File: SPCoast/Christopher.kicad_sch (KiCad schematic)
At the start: 42 parts, among them SW9813 813, SW9815 815, SW9817 817, SW9900 815A

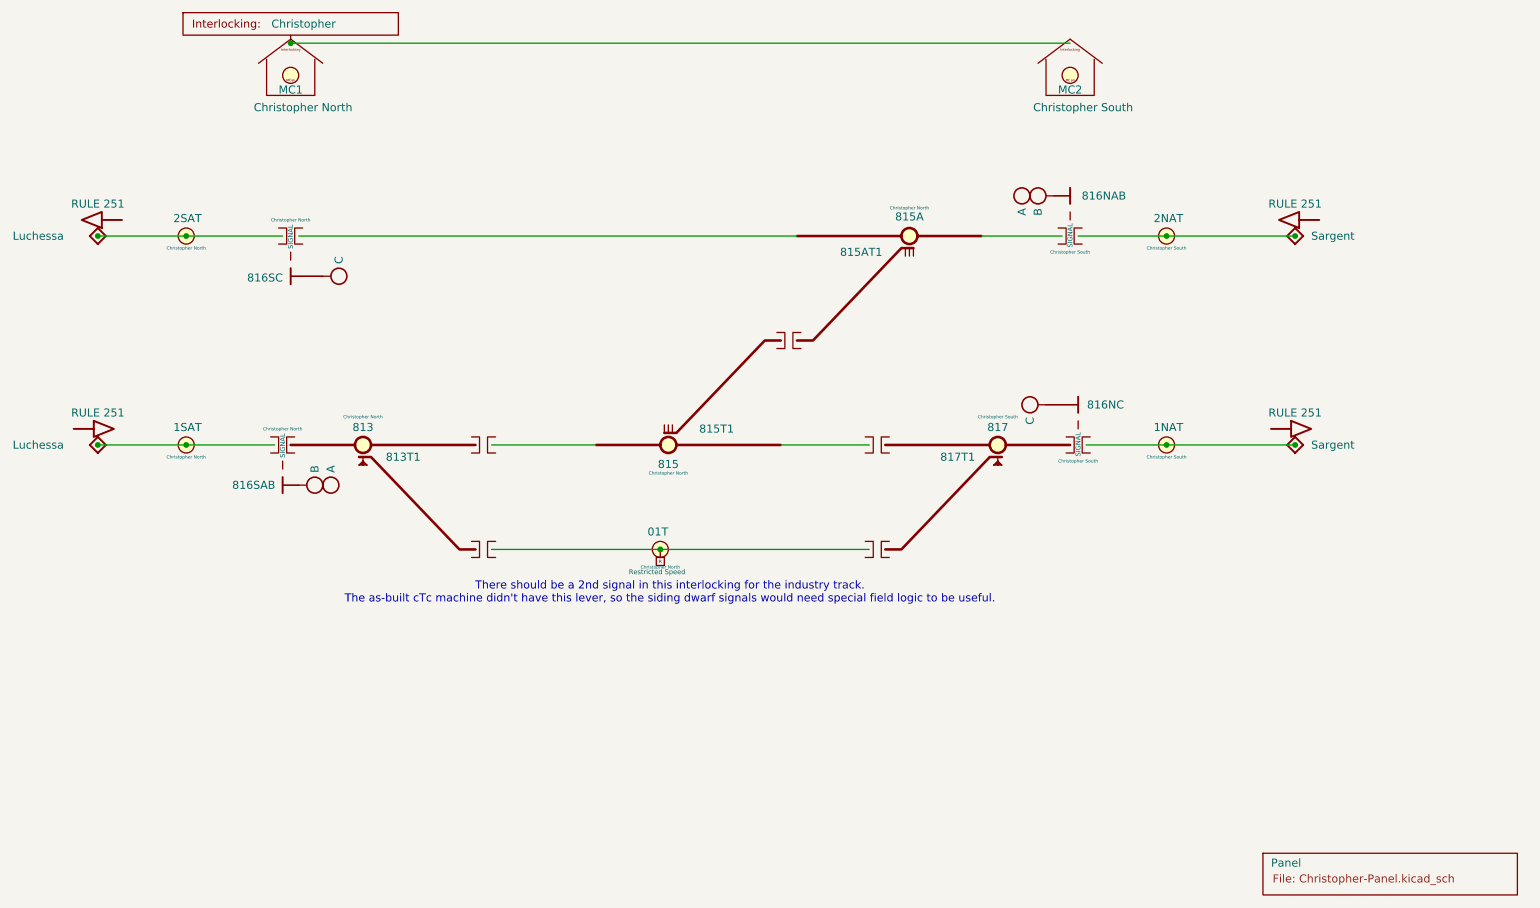
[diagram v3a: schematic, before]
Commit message: chore: owner's Sargent cleanup and library edits of 2026-10-12 and 13 (baseline)
Co-Authored-By: Claude Fable 5.1 <noreply@anthropic.com>
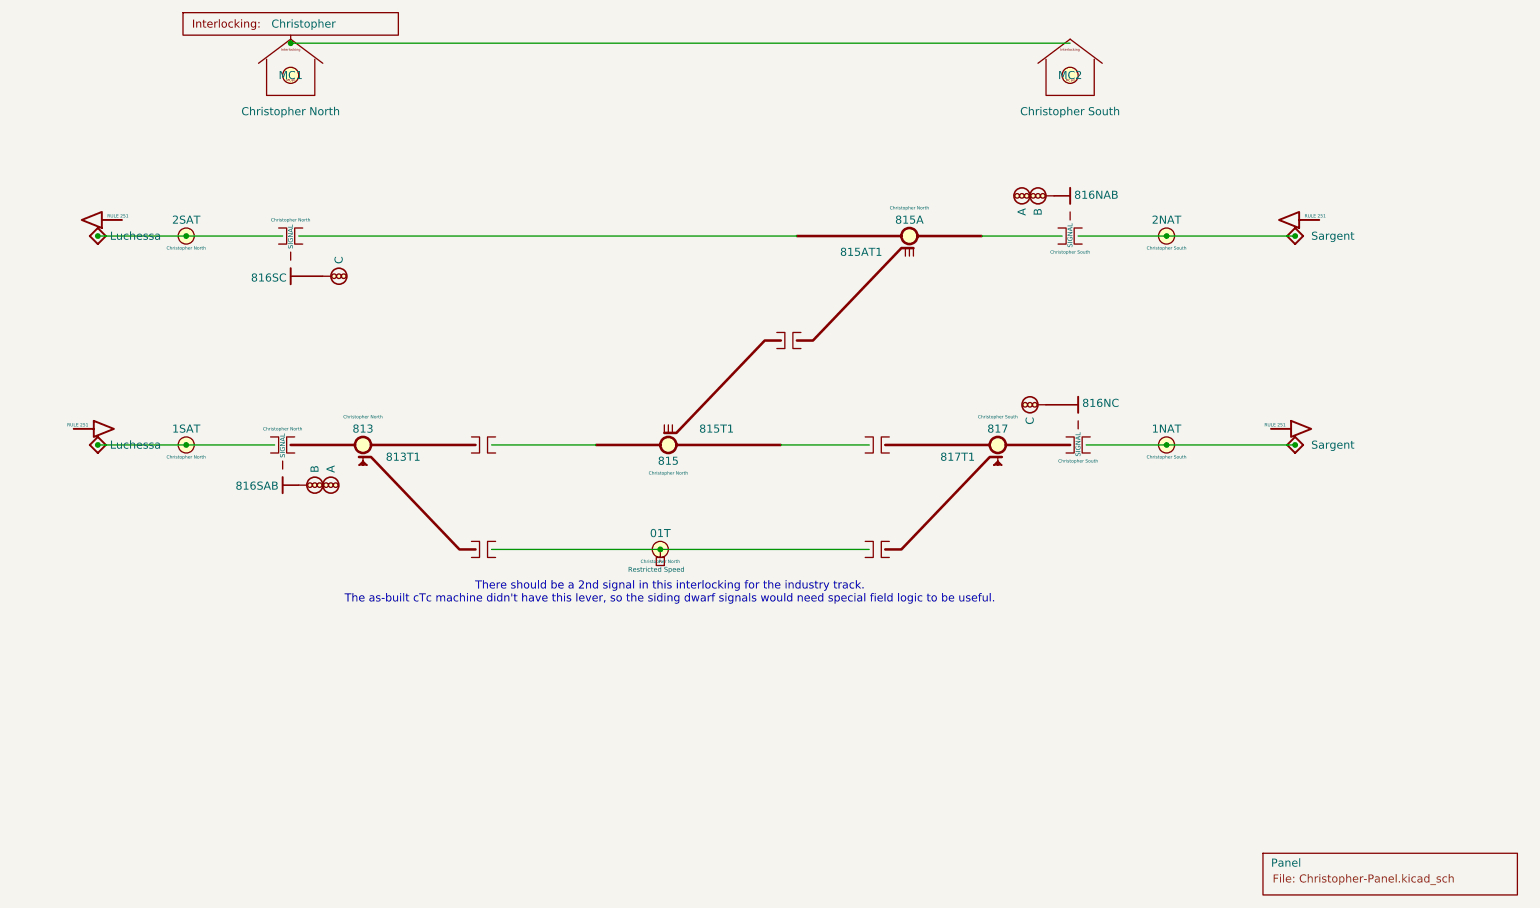
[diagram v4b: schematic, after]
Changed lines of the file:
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@@
 		)
 		(property "Value" "RULE 251"
-			(at 41.91 95.25 0)
+			(at 38.735 97.155 0)
 			(show_name no)
 			(do_not_autoplace yes)
 			(effects
 				(font
-					(size 1.27 1.27)
+					(size 0.508 0.508)
 					(color 0 0 0 1)
 				)
@@
 		(property "Value" ""
 			(at 151.13 83.82 0)
+			(hide yes)
 			(show_name no)
 			(do_not_autoplace no)
@@
 		)
 		(property "Value" "Christopher South"
-			(at 189.74 46.99 0)
+			(at 195.58 47.625 0)
 			(show_name no)
 			(do_not_autoplace no)
@@
 					(size 1.27 1.27)
 				)
-				(justify left)
 			)
 		)
@@
 		)
 		(property "Value" "1SAT"
-			(at 53.85 97.54 0)
+			(at 55.88 97.79 0)
 			(show_name no)
 			(do_not_autoplace no)
@@
 					(size 1.27 1.27)
 				)
-				(justify left)
 			)
 		)
@@
 		)
 		(property "Value" "816SC"
-			(at 68.326 73.914 0)
+			(at 71.755 73.914 0)
 			(show_name no)
-			(do_not_autoplace yes)
+			(do_not_autoplace no)
 			(effects
 				(font
 					(size 1.27 1.27)
 				)
+				(justify left)
 			)
 		)
@@
 		)
 		(property "Value" "815"
-			(at 132.08 103.38 0)
+			(at 132.08 102.87 0)
 			(show_name no)
 			(do_not_autoplace no)
@@
 			(at 145.415 99.695 0)
 			(show_name no)
-			(do_not_autoplace no)
+			(do_not_autoplace yes)
 			(effects
 				(font
@@
 		)
 		(property "Appliance" "switch"
-			(at 132.08 100.33 0)
+			(at 123.825 92.71 0)
 			(hide yes)
 			(show_name no)
@@
 		)
 		(property "Style" "powered"
-			(at 132.08 100.33 0)
+			(at 123.825 92.71 0)
 			(hide yes)
 			(show_name no)
@@
 		)
 		(property "Value" "813"
-			(at 83.82 97.54 0)
+			(at 83.82 97.79 0)
 			(show_name no)
 			(do_not_autoplace no)
@@
 			(at 97.155 100.965 0)
 			(show_name no)
-			(do_not_autoplace no)
+			(do_not_autoplace yes)
 			(effects
 				(font
@@
 		)
 		(property "Appliance" "switch"
-			(at 83.82 100.33 0)
+			(at 76.835 106.68 0)
 			(hide yes)
 			(show_name no)
@@
 		)
 		(property "Style" "lock"
-			(at 83.82 100.33 0)
+			(at 76.835 106.68 0)
 			(hide yes)
 			(show_name no)
@@
 		)
 		(property "Value" "Luchessa"
-			(at 28.448 100.33 0)
+			(at 43.815 100.33 0)
 			(show_name no)
 			(do_not_autoplace no)
@@
 		)
 		(property "Value" "816SAB"
-			(at 66.548 106.68 0)
+			(at 70.485 106.807 0)
 			(show_name no)
 			(do_not_autoplace yes)
@@
 					(size 1.27 1.27)
 				)
+				(justify left)
 			)
 		)
@@
 		)
 		(property "Value" "Restricted Speed"
-			(at 130.302 120.396 0)
+			(at 130.175 120.015 0)
 			(show_name no)
 			(do_not_autoplace yes)
@@
 		)
 		(property "Value" "MC1"
-			(at 72.39 44.196 0)
+			(at 72.39 41.91 0)
 			(show_name no)
 			(do_not_autoplace no)
@@
 		)
 		(property "Value" "01T"
-			(at 128.78 114.05 0)
+			(at 130.81 114.3 0)
 			(show_name no)
 			(do_not_autoplace no)
@@
 					(size 1.27 1.27)
 				)
-				(justify left)
 			)
 		)
@@
 		)
 		(property "CP" "Christopher North"
-			(at 130.81 119.634 0)
+			(at 130.81 118.745 0)
 			(show_name no)
 			(do_not_autoplace no)
@@
 		)
 		(property "Value" "Christopher North"
-			(at 66.55 46.99 0)
+			(at 72.39 47.625 0)
 			(show_name no)
 			(do_not_autoplace no)
@@
 					(size 1.27 1.27)
 				)
-				(justify left)
 			)
 		)
@@
 		)
 		(property "Value" "RULE 251"
-			(at 231.14 62.23 0)
+			(at 234.315 64.135 0)
 			(show_name no)
 			(do_not_autoplace yes)
 			(effects
 				(font
-					(size 1.27 1.27)
+					(size 0.508 0.508)
 					(color 0 0 0 1)
 				)
@@
 		)
 		(property "Value" "RULE 251"
-			(at 231.14 95.25 0)
+			(at 227.965 97.155 0)
 			(show_name no)
 			(do_not_autoplace yes)
 			(effects
 				(font
-					(size 1.27 1.27)
+					(size 0.508 0.508)
 					(color 0 0 0 1)
 				)
@@
 		)
 		(property "Value" "815A"
-			(at 170.18 64.26 0)
+			(at 170.18 64.77 0)
 			(show_name no)
 			(do_not_autoplace no)
@@
 			(at 156.845 67.945 0)
 			(show_name no)
-			(do_not_autoplace no)
+			(do_not_autoplace yes)
 			(effects
 				(font
@@
 		)
 		(property "Appliance" "switch"
-			(at 170.18 67.31 0)
+			(at 178.435 74.93 0)
 			(hide yes)
 			(show_name no)
@@
 		)
 		(property "Style" "powered"
-			(at 170.18 67.31 0)
+			(at 178.435 74.93 0)
 			(hide yes)
 			(show_name no)
@@
 		)
 		(property "Value" "MC2"
-			(at 195.58 44.196 0)
+			(at 195.58 41.91 0)
 			(show_name no)
 			(do_not_autoplace no)
@@
 		(property "Value" ""
 			(at 102.87 100.33 0)
+			(hide yes)
 			(show_name no)
 			(do_not_autoplace no)
@@
 		(property "Value" ""
 			(at 165.1 100.33 0)
+			(hide yes)
 			(show_name no)
 			(do_not_autoplace no)
@@
 		)
 		(property "Value" "2NAT"
-			(at 208.79 64.52 0)
+			(at 210.82 64.77 0)
 			(show_name no)
 			(do_not_autoplace no)
@@
 					(size 1.27 1.27)
 				)
-				(justify left)
 			)
 		)
@@
 		)
 		(property "Value" "816NC"
-			(at 201.168 93.98 0)
+			(at 197.485 93.726 0)
 			(show_name no)
-			(do_not_autoplace yes)
+			(do_not_autoplace no)
 			(effects
 				(font
 					(size 1.27 1.27)
 				)
+				(justify left)
 			)
 		)
@@
 		)
 		(property "Value" "1NAT"
-			(at 208.79 97.54 0)
+			(at 210.82 97.79 0)
 			(show_name no)
 			(do_not_autoplace no)
@@
 					(size 1.27 1.27)
 				)
-				(justify left)
 			)
 		)
@@
 		)
 		(property "Value" "817"
-			(at 184.15 97.54 0)
+			(at 184.15 97.79 0)
 			(show_name no)
 			(do_not_autoplace no)
@@
 			(at 170.815 100.965 0)
 			(show_name no)
-			(do_not_autoplace no)
+			(do_not_autoplace yes)
 			(effects
 				(font
@@
 		)
 		(property "Appliance" "switch"
-			(at 184.15 100.33 0)
+			(at 191.135 106.68 0)
 			(hide yes)
 			(show_name no)
@@
 		)
 		(property "Style" "lock"
-			(at 184.15 100.33 0)
+			(at 191.135 106.68 0)
 			(hide yes)
 			(show_name no)
@@
 		)
 		(property "Value" "816NAB"
-			(at 200.914 60.96 0)
+			(at 196.215 60.833 0)
 			(show_name no)
 			(do_not_autoplace yes)
@@
 					(size 1.27 1.27)
 				)
+				(justify left)
 			)
 		)
@@
 		)
 		(property "Value" "2SAT"
-			(at 53.85 64.52 0)
+			(at 55.88 64.77 0)
 			(show_name no)
 			(do_not_autoplace no)
@@
 					(size 1.27 1.27)
 				)
-				(justify left)
 			)
 		)
@@
 		)
 		(property "Value" "RULE 251"
-			(at 41.91 62.23 0)
+			(at 45.085 64.135 0)
 			(show_name no)
 			(do_not_autoplace yes)
 			(effects
 				(font
-					(size 1.27 1.27)
+					(size 0.508 0.508)
 					(color 0 0 0 1)
 				)
@@
 		)
 		(property "Value" "Luchessa"
-			(at 28.448 67.31 0)
+			(at 43.815 67.31 0)
 			(show_name no)
 			(do_not_autoplace no)

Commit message: fix(spcoast): placed instances agree with their library symbols on Role, Appliance, Style
KiCad copies fields at placement and never follows the library. The 2026-10-12 migration
filled empty instance fields but kept non-empty ones, so heads placed before the libraries
were corrected still said Role COMPONENT and Style CPL. A compiler joining devices to
appliances by Appliance and Style (I9) would have failed on Sargent's CL and UQ heads.

The one-off `SPCoast/edits/2026-10-16-sync-library-fields.py` sets every library-owned
field (Role, Appliance, Style, IC, Kind, Pin.*) on every instance of a Railroad-* symbol
to the library's value, by text edit. 58 instances on 7 sheets: 53 heads to Role APPLIANCE
(Sargent's H1 to Style UQ and H2 to CL), two Mileposts to Role TRACK (ADR 0004 D7), the
Sargent Local plates to Role DEVICE (checkpoint E72), and 836SB's semaphore device to the
library's Style list `LQ, UQ`.

Front-end rule this records (owner, 2026-10-16): library-owned fields are read from the
library by lib_id, and an instance that disagrees is a diagnostic.

Verified:
- tools/contract/netlist_diff.py production/SPCoast.net production/post-sync.net: 493 nets,
  1086 nodes, 485 parts, connectivity identical
- kicad-cli sch erc --severity-all: 0 violations
- the script re-run reports 0 changes

Co-Authored-By: Claude Fable 5.1 <noreply@anthropic.com>
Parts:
- H9003, H9005, H9006, H9008, H9009, H9010: Role COMPONENT -> APPLIANCE
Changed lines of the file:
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@@
 			)
 		)
-		(property "Role" "COMPONENT"
+		(property "Role" "APPLIANCE"
 			(at 194.31 63.5 0)
 			(hide yes)
@@
 			)
 		)
-		(property "Role" "COMPONENT"
+		(property "Role" "APPLIANCE"
 			(at 193.04 96.52 0)
 			(hide yes)
@@
 			)
 		)
-		(property "Role" "COMPONENT"
+		(property "Role" "APPLIANCE"
 			(at 74.93 104.14 0)
 			(hide yes)
@@
 			)
 		)
-		(property "Role" "COMPONENT"
+		(property "Role" "APPLIANCE"
 			(at 72.39 104.14 0)
 			(hide yes)
@@
 			)
 		)
-		(property "Role" "COMPONENT"
+		(property "Role" "APPLIANCE"
 			(at 76.2 71.12 0)
 			(hide yes)
@@
 			)
 		)
-		(property "Role" "COMPONENT"
+		(property "Role" "APPLIANCE"
 			(at 191.77 63.5 0)
 			(hide yes)
